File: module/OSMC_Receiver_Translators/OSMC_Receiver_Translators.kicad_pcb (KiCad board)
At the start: 4 copper layers, 120.1 x 78.2 mm, 67 parts, among them U1 24AA02-OT, U13 OSMC Module Board, U14 OSMC Module Board, U15 OSMC Module Board, U16 OSMC Module Board, U17 OSMC Module Board, U18 OSMC Module Board, U19 OSMC Module Board, U2 LTC4317, U20 OSMC Module Board, U3 XIAO-ESP32-S3-DIP, U4 PCF8574DWR, U5 LTC4317, U6 LTC4317, U7 LTC4317

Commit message: reviewed PCBs
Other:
- board text added: "Reciever Translate V1 02/26"
- board text removed: "Module Reciever V1 02/26"
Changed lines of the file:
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@@
 		(layer "Edge.Cuts")
 	)
-	(gr_text "Module Reciever V1\n02/26"
+	(gr_text "Reciever Translate V1\n02/26"
 		(at 190.51 100.71 0)
 		(layer "F.SilkS")

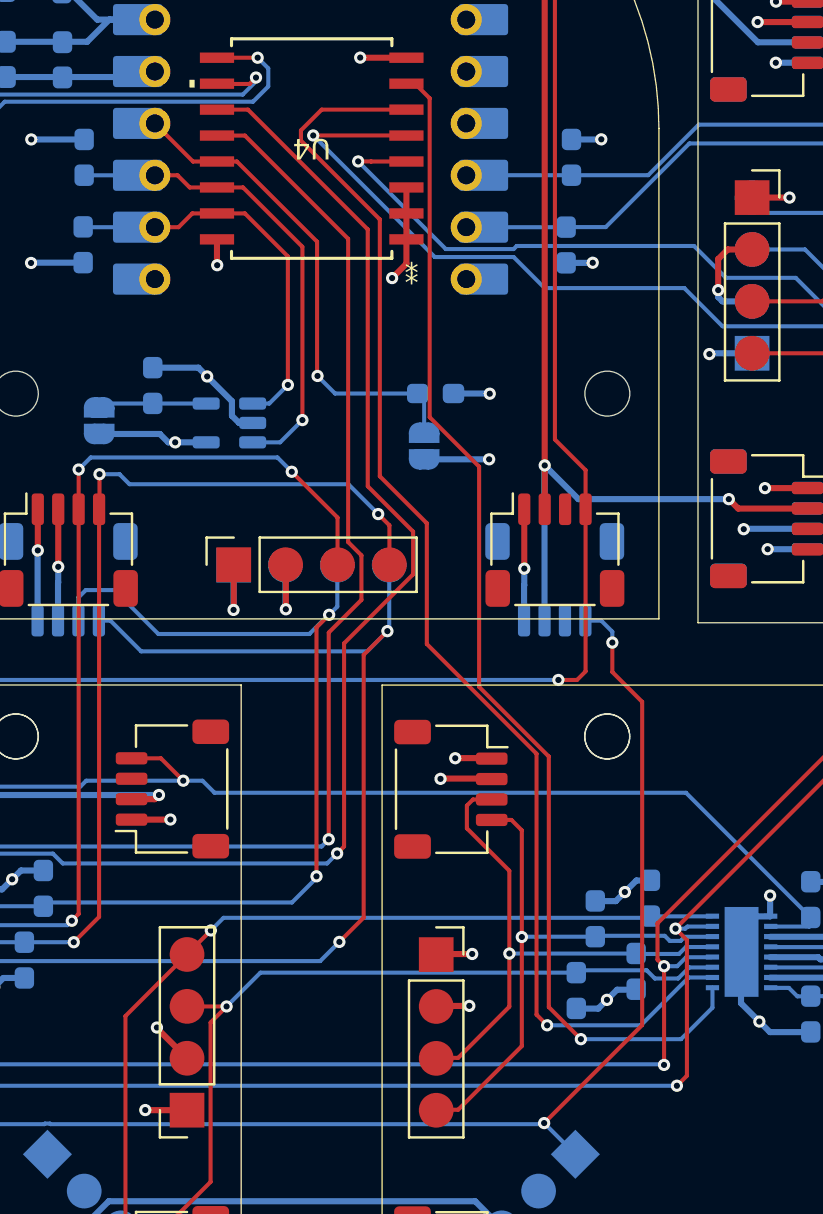
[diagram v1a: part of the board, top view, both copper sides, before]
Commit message: update to pcb, fixed i2c lines for bus 0 and 1
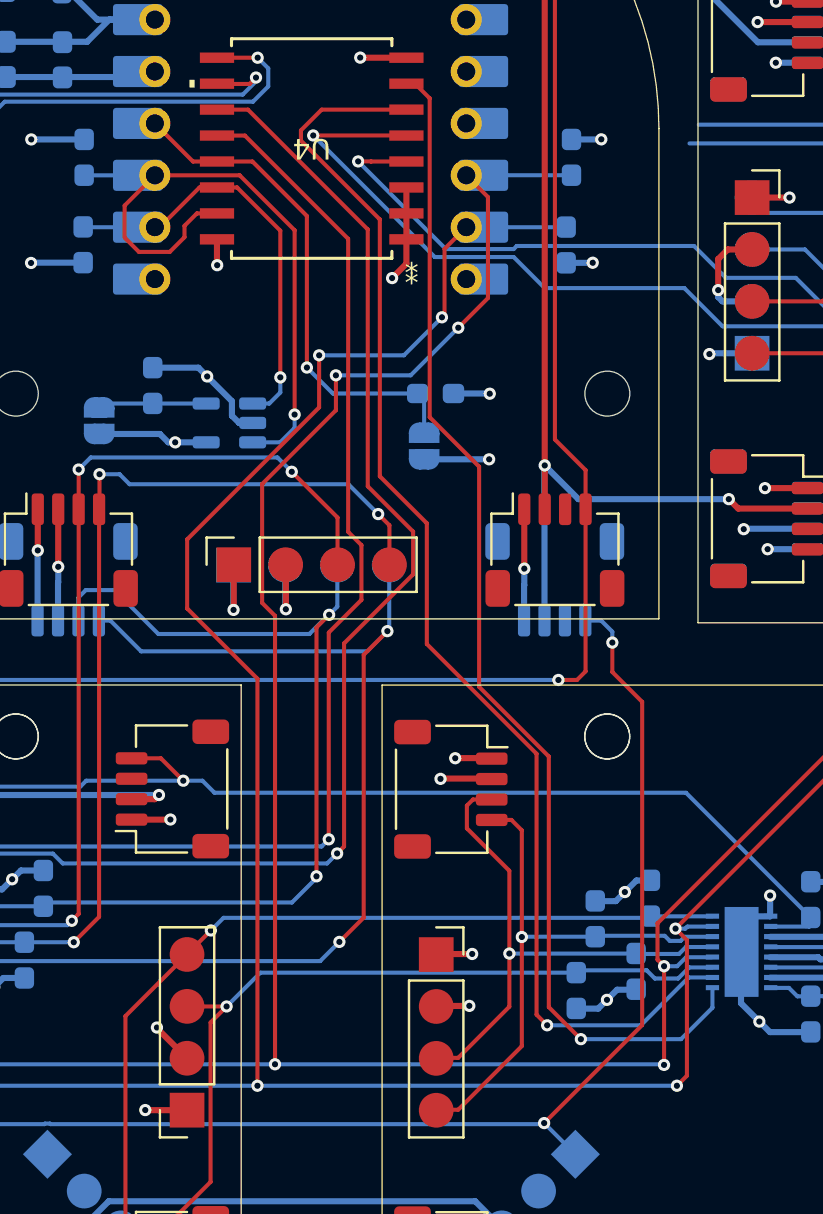
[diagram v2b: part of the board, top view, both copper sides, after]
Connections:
- U4 pad 14: /SDA1 -> /SCL1
- U4 pad 15: /SCL1 -> /SDA1
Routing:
- net /SCL: track 172.2 -> 216.0 mm, vias 7 -> 10
- net /SDA: track 172.6 -> 216.3 mm, vias 7 -> 10
- net /SDA1: track 23.5 -> 33.0 mm
- net /SCL1: track 19.6 -> 20.8 mm
- net /INT: track 24.2 -> 24.7 mm

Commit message: board update
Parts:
- added J1: Conn_01x04, OSMC_Module:CONN4_BM04B-SRSS_JST, F.Cu at (102.8, 26.0)
- added J10: Conn_01x04, OSMC_Module:CONN4_BM04B-SRSS_JST, F.Cu at (121.2, 32.0)
- added J11: Conn_01x04, OSMC_Module:CONN4_BM04B-SRSS_JST, F.Cu at (121.2, 38.0)
- added J12: Conn_01x04, OSMC_Module:CONN4_BM04B-SRSS_JST, F.Cu at (121.2, 43.9)
- added J13: Conn_01x04, OSMC_Module:CONN4_BM04B-SRSS_JST, F.Cu at (130.3, 26.0)
- added J14: Conn_01x04, OSMC_Module:CONN4_BM04B-SRSS_JST, F.Cu at (130.3, 32.0)
- added J15: Conn_01x04, OSMC_Module:CONN4_BM04B-SRSS_JST, F.Cu at (130.3, 38.0)
- added J16: Conn_01x04, OSMC_Module:CONN4_BM04B-SRSS_JST, F.Cu at (130.3, 43.9)
- added J2: Conn_01x04, OSMC_Module:CONN4_BM04B-SRSS_JST, F.Cu at (102.8, 32.0)
- added J3: Conn_01x04, OSMC_Module:CONN4_BM04B-SRSS_JST, F.Cu at (102.8, 38.0)
- added J4: Conn_01x04, OSMC_Module:CONN4_BM04B-SRSS_JST, F.Cu at (102.8, 43.9)
- added J5: Conn_01x04, OSMC_Module:CONN4_BM04B-SRSS_JST, F.Cu at (112.0, 26.0)
- added J6: Conn_01x04, OSMC_Module:CONN4_BM04B-SRSS_JST, F.Cu at (112.0, 32.0)
- added J7: Conn_01x04, OSMC_Module:CONN4_BM04B-SRSS_JST, F.Cu at (112.0, 38.0)
- added J8: Conn_01x04, OSMC_Module:CONN4_BM04B-SRSS_JST, F.Cu at (112.0, 43.9)
- added J9: Conn_01x04, OSMC_Module:CONN4_BM04B-SRSS_JST, F.Cu at (121.2, 26.0)
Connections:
- U17 pad 3: /Modules/SCL4 -> /Modules/SDA4
- U17 pad 4: /Modules/SDA4 -> /Modules/SCL4
- U17 pad 7: /Modules/SCL4 -> /Modules/SDA4
- U17 pad 8: /Modules/SDA4 -> /Modules/SCL4
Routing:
- net /Modules/SCL4: track 31.2 -> 30.1 mm
- net /Modules/SDA4: track 30.9 -> 31.4 mm
